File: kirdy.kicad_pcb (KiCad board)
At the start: 2 copper layers, 384 parts, among them J1 MOD_IN, J2 DNP, J3 DNP, J4 Conn_02x05_Odd_Even, J5 Barrel_Jack, J6 RJ45_Abracon_ARJP11A-MASA-B-A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, J7 USB_C_Receptacle_USB2.0, J8 Conn_02x05_Odd_Even, J9 Conn_02x05_Odd_Even, Q1 CSD17507Q5A, Q2 BSS138, Q3 BSS138, Q4 BC857, Q5 AOSP21321, Q6 BC857, SW1 SW_DIP_x03, U1 LTC6655BHLS8-4.096, U10 LT3081xDF, U11 LT3042xMSE, U12 LT3045xMSE, U13 LT3045xMSE, U14 LT3042xMSE, U15 LT3094xMSE, U16 LT3042xMSE, U17 AD5680, U18 AD7172-2, U19 RS8552, U2 MAX5719xSD, U20 MAX1968xUI, U21 ACPL-217-500E, U22 TPS54620, U23 AG5300, U24 ACPL-217-500E, U25 AMS1117-3.3, U26 LAN8742A, U27 USBLC6-4SC6, U28 USBLC6-4SC6, U3 ADA4898-1YRDZ, U4 ADA4898-1YRDZ, U5 RS8552, U6 ADA4898-1YRDZ, U7 STM32F407VGTx, U8 STM809SWX6F, U9 LTC3261, Y1 8MHz, Y2 25MHz

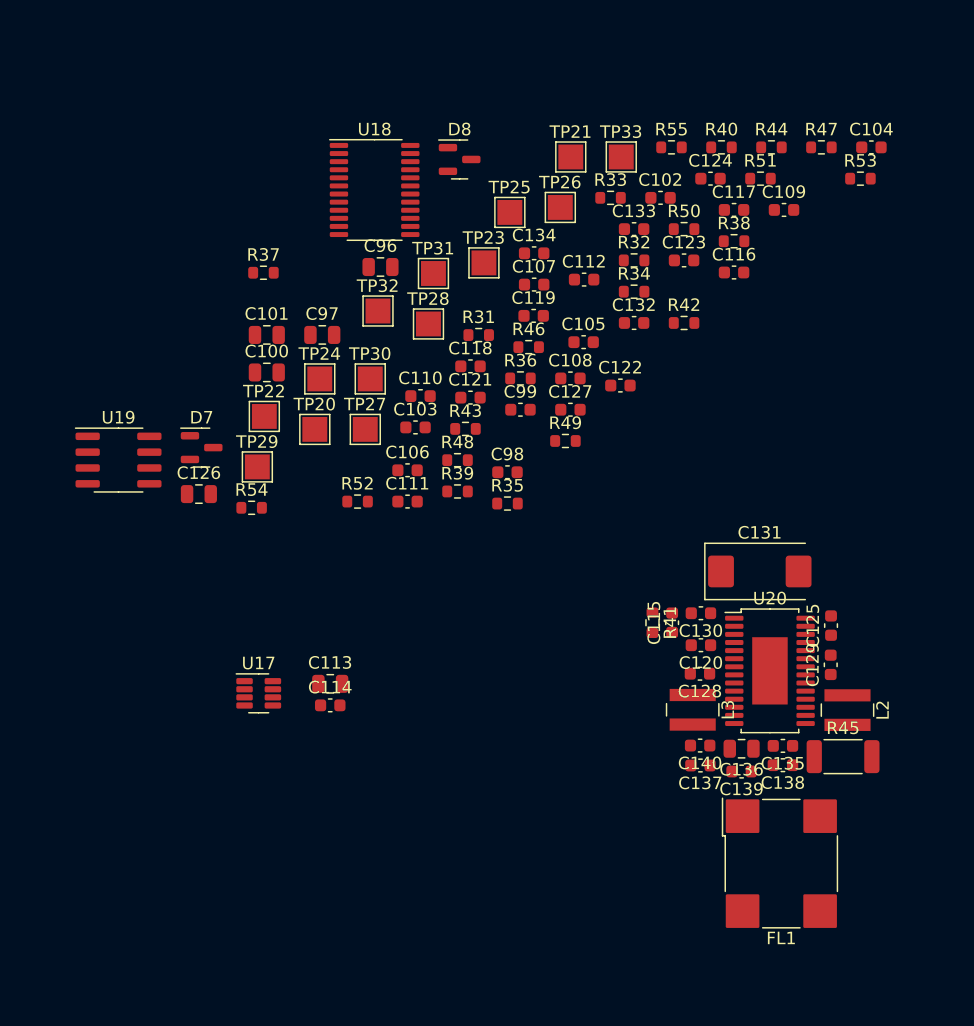
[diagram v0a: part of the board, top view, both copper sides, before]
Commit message: add bom, finish rough placement
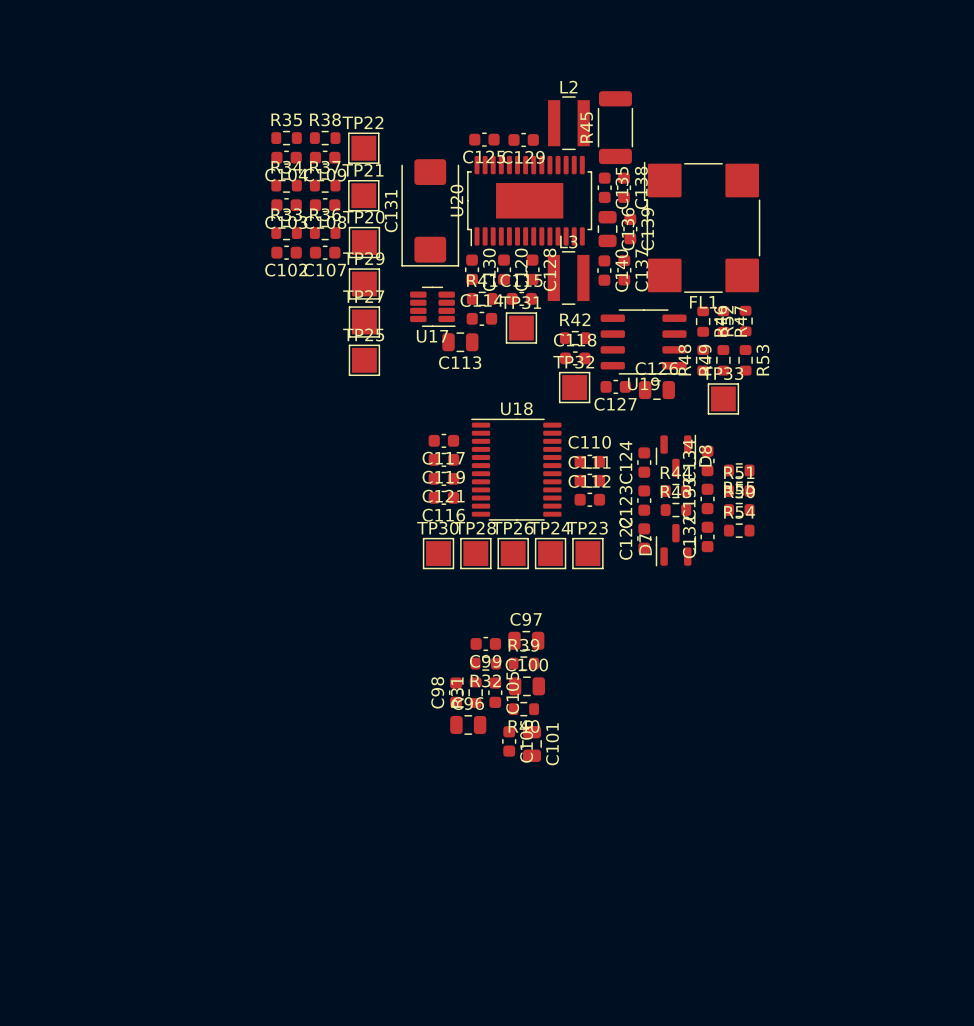
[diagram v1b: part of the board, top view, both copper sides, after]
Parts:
- FL1: value 5A -> WE-SL5
- moved R45 53.7 mm to (359.3, 86.5), turned to 90 degrees
- moved L2 52.1 mm to (355.6, 86.1), turned to 0 degrees
- moved FL1 51.4 mm to (366.4, 94.5)
- moved C129 48.8 mm to (352.0, 87.5), turned to 180 degrees
- moved C138 48.1 mm to (360.0, 91.3), turned to -90 degrees
- moved C125 47.9 mm to (348.8, 87.5), turned to 180 degrees
- moved R40 47.8 mm to (352.0, 133.1), turned to 180 degrees
- moved C135 47.0 mm to (358.5, 91.3), turned to -90 degrees
- moved C104 46.9 mm to (332.9, 88.9), turned to 180 degrees
- moved C139 44.4 mm to (360.5, 94.6), turned to -90 degrees
- moved U19 43.2 mm to (361.6, 103.7), turned to 180 degrees
- moved C136 43.1 mm to (358.7, 94.6), turned to -90 degrees
- moved U20 42.4 mm to (352.5, 92.4), turned to 90 degrees
- moved C137 40.2 mm to (360.0, 97.9), turned to -90 degrees
- moved C131 39.2 mm to (344.5, 93.2), turned to 90 degrees
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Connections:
- FL1 pad 2: /thermostat/TEC+ -> Net-(C136-Pad2)
- FL1 pad 3: Net-(C136-Pad2) -> /thermostat/TEC-
- FL1 pad 4: /thermostat/TEC- -> /thermostat/TEC+

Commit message: complete placement
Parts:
- added C173: 100n, Capacitor_SMD:C_0603_1608Metric, F.Cu at (77.8, 38.9)
- added H1: MountingHole_Pad, MountingHole:MountingHole_2.7mm_M2.5_Pad_Via, F.Cu at (3.57, 5.51)
- added H2: MountingHole_Pad, MountingHole:MountingHole_2.7mm_M2.5_Pad_Via, F.Cu at (3.56, 94.4)
- added H3: MountingHole_Pad, MountingHole:MountingHole_2.7mm_M2.5_Pad_Via, F.Cu at (156.0, 96.0)
- added H4: MountingHole_Pad, MountingHole:MountingHole_2.7mm_M2.5_Pad_Via, F.Cu at (156.0, 4.00)
- added R100: 0, Resistor_SMD:R_0603_1608Metric, F.Cu at (153.7, 91.7)
- added R101: 0, Resistor_SMD:R_0603_1608Metric, F.Cu at (156.0, 8.36)
- added R98: 0, Resistor_SMD:R_0603_1608Metric, F.Cu at (8.87, 7.83)
- added R99: 0, Resistor_SMD:R_0603_1608Metric, F.Cu at (8.56, 92.8)
- FL3: value 90R@100MHz -> Filter_EMI_LL_1423
- TP1, TP10, TP11, TP12, TP13, TP14, TP15, TP16, TP17, TP18, TP19, TP2, TP20, TP21, TP22, TP23, TP24, TP25, TP26, TP27, TP28, TP29, TP3, TP30, TP31, TP32, TP33, TP34, TP35, TP36, TP37, TP38, TP4, TP5, TP6, TP7, TP8, TP9: moved to B.Cu
- moved TP14 397.3 mm to (69.8, 31.8), turned to 180 degrees
- moved C63 395.7 mm to (72.4, 42.5), turned to 180 degrees
- moved C46 395.6 mm to (76.7, 51.5), turned to 90 degrees
- moved C83 394.9 mm to (66.3, 39.1), turned to -90 degrees
- moved C50 394.9 mm to (68.9, 46.5)
- moved C76 393.1 mm to (68.9, 34.6)
- moved C57 390.7 mm to (68.9, 44.4)
- moved TP13 390.0 mm to (78.7, 47.0), turned to 180 degrees
- moved C69 389.8 mm to (71.7, 40.1), turned to -90 degrees
- moved R23 389.7 mm to (71.7, 37.0), turned to -90 degrees
- moved C75 388.6 mm to (81.0, 41.9)
- moved C90 387.5 mm to (66.3, 35.6), turned to 90 degrees
- moved C35 387.5 mm to (88.4, 56.2), turned to -90 degrees
- moved C36 386.5 mm to (79.4, 55.5), turned to 90 degrees
- moved C66 385.2 mm to (91.8, 45.6), turned to -90 degrees
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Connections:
- net +1V8 renamed Net-(C35-Pad1)
- FL3 pad 1: Net-(FL3-Pad1) -> Net-(J7-PadA6)
- FL3 pad 2: Net-(FL3-Pad2) -> /MCU/USB_DP
- FL3 pad 3: /MCU/USB_DP -> /MCU/USB_DN
- FL3 pad 4: /MCU/USB_DN -> Net-(J7-PadA7)
- J3 pad 1: GND -> Net-(J3-Pad1)
- J7 pad A6: Net-(FL3-Pad2) -> Net-(J7-PadA6)
- J7 pad A7: Net-(FL3-Pad1) -> Net-(J7-PadA7)
- J7 pad B6: Net-(FL3-Pad2) -> Net-(J7-PadA6)
- J7 pad B7: Net-(FL3-Pad1) -> Net-(J7-PadA7)
- R13 pad 3: GND -> Net-(J3-Pad1)
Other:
- board outline added: 160 x 100 mm

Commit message: routing, bom update
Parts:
- added R102: 1k, Resistor_SMD:R_0603_1608Metric, F.Cu at (40.9, 41.1)
- moved TP23 10.3 mm to (138.4, 97.2)
- moved TP24 10.3 mm to (142.2, 97.2)
- moved TP30 10.3 mm to (134.5, 97.2)
- moved TP26 10.3 mm to (142.2, 101.0)
- moved TP28 10.3 mm to (134.5, 101.0)
- moved C169 10.2 mm to (30.5, 50.6), turned to 90 degrees
- moved TP32 7.31 mm to (121.4, 62.3)
- moved C146 5.46 mm to (39.8, 80.0), turned to 180 degrees
- moved C8 3.63 mm to (121.4, 28.3), turned to -90 degrees
- moved TP33 2.55 mm to (134.6, 64.4)
- moved R3 1.53 mm to (109.2, 26.3)
- moved C170 1.51 mm to (24.8, 59.2)
- moved D1 1.06 mm to (110.3, 10.7)
- moved R1 1.06 mm to (107.5, 11.5)
- moved R2 1.06 mm to (110.3, 12.5)
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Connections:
- J9 pad 7: /thermostat/NTC+ -> /thermostat/NTC-
- J9 pad 9: /thermostat/NTC- -> /thermostat/NTC+
- U27 pad 4: /Ehternet/PHY_TD_P -> /Ehternet/PHY_TD_N
- U27 pad 6: /Ehternet/PHY_TD_N -> /Ehternet/PHY_TD_P
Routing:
- net /MCU/TADC_SYNC: track 0.00 -> 129.7 mm, vias 0 -> 2
- net /MCU/TADC_MISO: track 0.00 -> 126.7 mm, vias 0 -> 2
- net /MCU/TADC_CLK: track 0.00 -> 125.9 mm, vias 0 -> 2
- net /MCU/TEC_VSEN: track 0.00 -> 122.4 mm, vias 0 -> 2
- net /MCU/TADC_MOSI: track 0.00 -> 122.4 mm, vias 0 -> 2
- net /MCU/TADC_CS: track 0.00 -> 120.8 mm, vias 0 -> 2
- net Net-(J1-Pad1): track 0.00 -> 118.3 mm
- net /MCU/PD_MON: track 0.00 -> 116.6 mm
- net /MCU/TEC_SHDN: track 0.00 -> 112.5 mm, vias 0 -> 2
- net /MCU/TEC_ISEN: track 0.00 -> 111.3 mm, vias 0 -> 2
- net /MCU/TDAC_MOSI: track 0.00 -> 110.5 mm, vias 0 -> 2
- net /MCU/TEC_VREF: track 0.00 -> 107.3 mm, vias 0 -> 2
- net /MCU/TDAC_CLK: track 0.00 -> 105.3 mm, vias 0 -> 2
- net /MCU/TDAC_SYNC: track 0.00 -> 101.3 mm, vias 0 -> 2
- net /MCU/PD_BIAS: track 0.00 -> 99.8 mm, vias 0 -> 2
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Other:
- copper layers 2 -> 4

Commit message: more routing
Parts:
- removed TP1, TP11, TP12, TP13, TP14, TP15, TP16, TP17, TP18, TP19, TP2, TP20, TP21, TP22, TP23, TP24, TP25, TP26, TP27, TP28, TP29, TP3, TP30, TP31, TP32, TP33, TP34, TP35, TP36, TP37, TP38, TP4, TP5, TP6, TP7, TP8: TestPoint, TestPoint:TestPoint_Pad_2.0x2.0mm
- J5: value Barrel_Jack -> Barrel_Jack_MountingPin
- R62: footprint Resistor_SMD:R_0603_1608Metric -> Resistor_SMD:R_1206_3216Metric
- moved R62 34.0 mm to (13.7, 89.5), turned to 90 degrees
- moved Q3 30.8 mm to (16.6, 89.9)
- moved R91 22.7 mm to (13.5, 52.7), turned to 90 degrees
- moved C171 20.4 mm to (16.9, 53.1)
- moved TP9 14.9 mm to (136.1, 16.8)
- moved TP10 13.1 mm to (137.9, 13.2)
- moved C152 3.57 mm to (70.9, 83.8), turned to 180 degrees
- moved C155 3.44 mm to (70.9, 79.0), turned to 180 degrees
- moved D9 2.89 mm to (14.4, 80.9)
- moved R68 2.44 mm to (76.5, 81.5)
- moved R69 2.44 mm to (76.5, 78.2)
- moved C46 2.18 mm to (74.5, 51.2)
- moved C44 2.16 mm to (78.4, 51.3)
- moved C45 2.16 mm to (76.3, 51.3)
- moved C33 2.16 mm to (73.4, 55.3)
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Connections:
- J5 pad MP: (no net) -> GND
- J6 pad 10: /Ehternet/POE_VC+ -> /Ehternet/POE_VC-
- J6 pad 9: /Ehternet/POE_VC- -> /Ehternet/POE_VC+
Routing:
- net /MCU/MCU_RSTn: track 2.15 -> 94.1 mm
- net /Ehternet/POE_VC-: track 4.02 -> 53.3 mm, vias 0 -> 2
- net /Ehternet/POE_VC+: track 0.00 -> 44.9 mm, vias 0 -> 2
- net Net-(Q3-Pad1): track 24.3 -> 56.4 mm, vias 0 -> 2
- net /Ehternet/ETH_SHIELD: track 31.8 -> 0.00 mm
- net Net-(U23-Pad3): track 0.00 -> 29.5 mm, vias 0 -> 1
- net /MCU/TEC_SHDN: track 112.5 -> 140.2 mm, vias 2 -> 4
- net /thermostat/ADC_REF: track 6.68 -> 33.7 mm, vias 0 -> 2
- net +5V: track 4.56 -> 31.3 mm, vias 0 -> 6
- net Net-(Q6-Pad1): track 0.00 -> 20.9 mm, vias 0 -> 2
- net Net-(C145-Pad2): track 19.5 -> 0.00 mm
- net /MCU/TDAC_MOSI: track 110.5 -> 126.4 mm
- net /MCU/TDAC_CLK: track 105.3 -> 121.3 mm
- net /MCU/TDAC_SYNC: track 101.3 -> 117.3 mm
- net Net-(C146-Pad1): track 0.00 -> 15.7 mm, vias 0 -> 2
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- added copper zone on F.Cu, net +12V
- added copper zone on F.Cu, net +15V
- added copper zone on F.Cu, net +3.3VA
- added copper zone on F.Cu, net +5V
- added copper zone on F.Cu, net +5VA
- added copper zone on F.Cu, net +8V
- added copper zone on F.Cu, net +9V
- added copper zone on F.Cu, net +9VA
- added copper zone on F.Cu, net -6V
- added copper zone on F.Cu, net -9V
- added copper zone on B.Cu, net /Ehternet/ETH_SHIELD
- added copper zone on F.Cu, net /Ehternet/ETH_SHIELD
- added copper zone on F.Cu, net /Ehternet/POE_VC+
- added copper zone on F.Cu, net /Ehternet/POE_VC-
- added copper zone on F.Cu, net /driveStage/LD-
- added copper zone on F.Cu, net /thermostat/TEC+
- added copper zone on F.Cu, net /thermostat/TEC-
- added copper zone on In1.Cu, net GND
- added copper zone on F.Cu, net IN
- added copper zone on F.Cu, net Net-(C135-Pad2)
- added copper zone on F.Cu, net Net-(C136-Pad2)
- added copper zone on F.Cu, net Net-(C141-Pad1)
- added copper zone on F.Cu, net Net-(C145-Pad1)
- added copper zone on F.Cu, net Net-(C145-Pad2)
- added copper zone on F.Cu, net Net-(C146-Pad1)
- added copper zone on F.Cu, net Net-(C148-Pad1)
- added copper zone on F.Cu, net Net-(C149-Pad2)
- added copper zone on F.Cu, net Net-(C152-Pad1)
- added copper zone on F.Cu, net Net-(C152-Pad2)
- added copper zone on F.Cu, net Net-(C35-Pad1)
- added copper zone on F.Cu, net Net-(C37-Pad2)
- added copper zone on F.Cu, net Net-(C40-Pad1)
- added copper zone on F.Cu, net Net-(C42-Pad2)
- added copper zone on F.Cu, net Net-(C43-Pad2)
- added copper zone on F.Cu, net Net-(C50-Pad1)
- added copper zone on F.Cu, net Net-(C51-Pad1)
- added copper zone on F.Cu, net Net-(C52-Pad1)
- added copper zone on F.Cu, net Net-(C53-Pad1)
- added copper zone on F.Cu, net Net-(C54-Pad1)
- added copper zone on F.Cu, net Net-(C55-Pad1)
- added copper zone on F.Cu, net Net-(L2-Pad1)
- added copper zone on F.Cu, net Net-(L3-Pad1)
- added copper zone on F.Cu, net Net-(Q1-Pad1)
- added copper zone on F.Cu, net Net-(R45-Pad1)

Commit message: roughly done
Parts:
- TP10, TP9: moved to F.Cu
- moved TP9 7.73 mm to (130.4, 11.6), turned to 0 degrees
- moved R98 5.62 mm to (3.56, 9.65)
- moved R99 5.60 mm to (3.56, 90.3)
- moved TP10 4.62 mm to (133.6, 11.6), turned to 0 degrees
- moved R100 2.39 mm to (156.1, 91.6), turned to 180 degrees
- moved L2 0.22 mm to (120.6, 68.1)
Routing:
- net GND: track 16.4 -> 377.1 mm, vias 0 -> 441
- net +3V3: track 21.9 -> 48.2 mm, vias 0 -> 41
- net Net-(U19-Pad5): track 0.00 -> 18.8 mm, vias 0 -> 2
- net +3.3VA: track 3.90 -> 17.3 mm, vias 0 -> 15
- net Net-(R10-Pad2): track 1.78 -> 10.5 mm
- net Net-(Q5-Pad4): track 2.15 -> 8.06 mm
- net Net-(J2-Pad1): track 7.66 -> 13.2 mm
- net +5VA: track 13.7 -> 19.3 mm, vias 0 -> 9
- net Net-(H3-Pad1): track 0.00 -> 4.81 mm
- net Net-(H4-Pad1): track 0.00 -> 4.71 mm
- net Net-(H1-Pad1): track 0.00 -> 4.49 mm
- net Net-(H2-Pad1): track 0.00 -> 4.46 mm
- net /MCU/PD_BIAS: track 99.9 -> 103.4 mm
- net -6V: track 15.9 -> 13.5 mm, vias 0 -> 29
- net +9VA: track 10.3 -> 12.5 mm, vias 0 -> 9
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- added copper zone on In2.Cu, net +12V
- added copper zone on B.Cu, net +15V
- added copper zone on In2.Cu, net +3.3VA
- added copper zone on F.Cu, net +3V3
- added copper zone on In2.Cu, net +3V3
- added copper zone on In2.Cu, net +5V
- added copper zone on In2.Cu, net +5VA
- added copper zone on In2.Cu, net +9V
- added copper zone on B.Cu, net +9VA
- added copper zone on In2.Cu, net -6V
- added copper zone on F.Cu, net Net-(C158-Pad1)

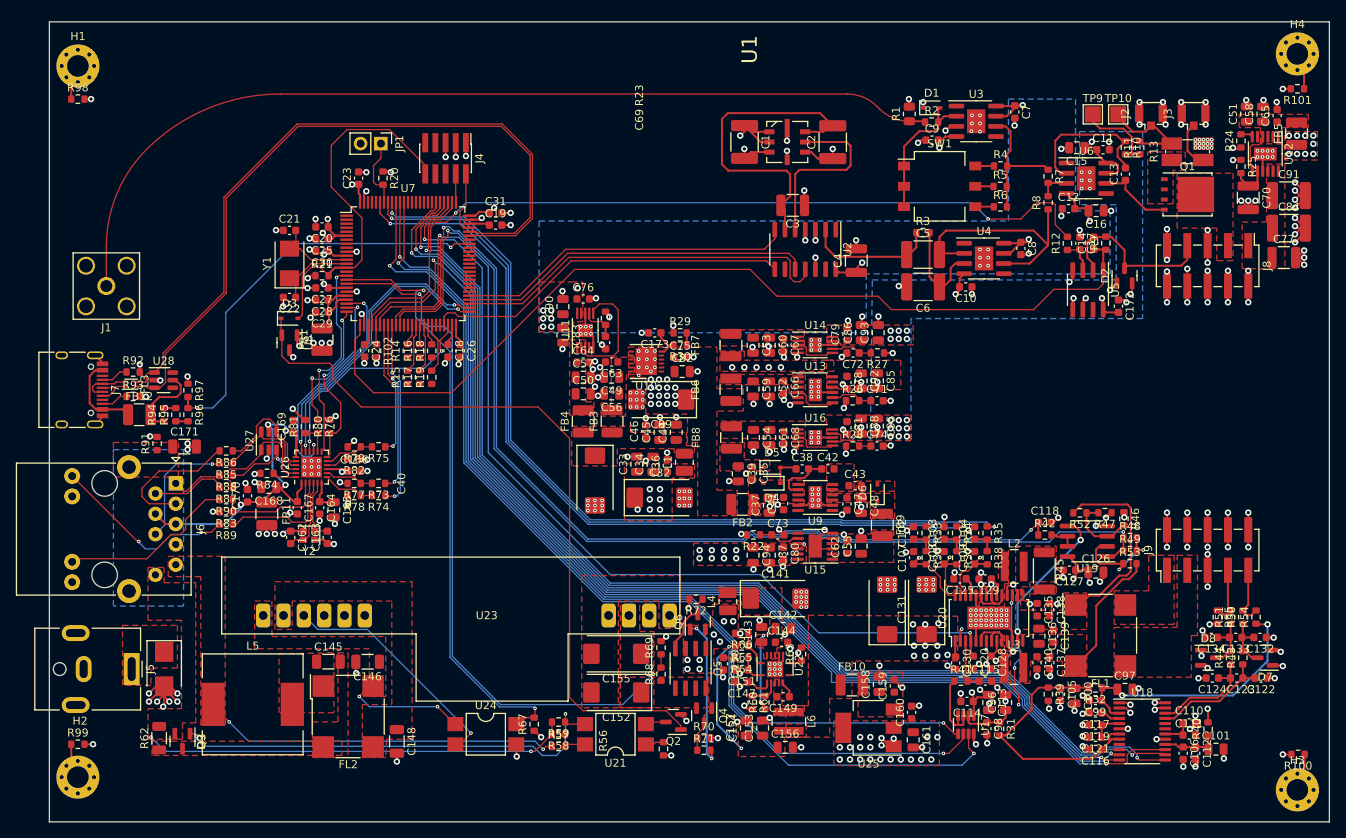
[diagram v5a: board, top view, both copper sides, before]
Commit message: passes DRC
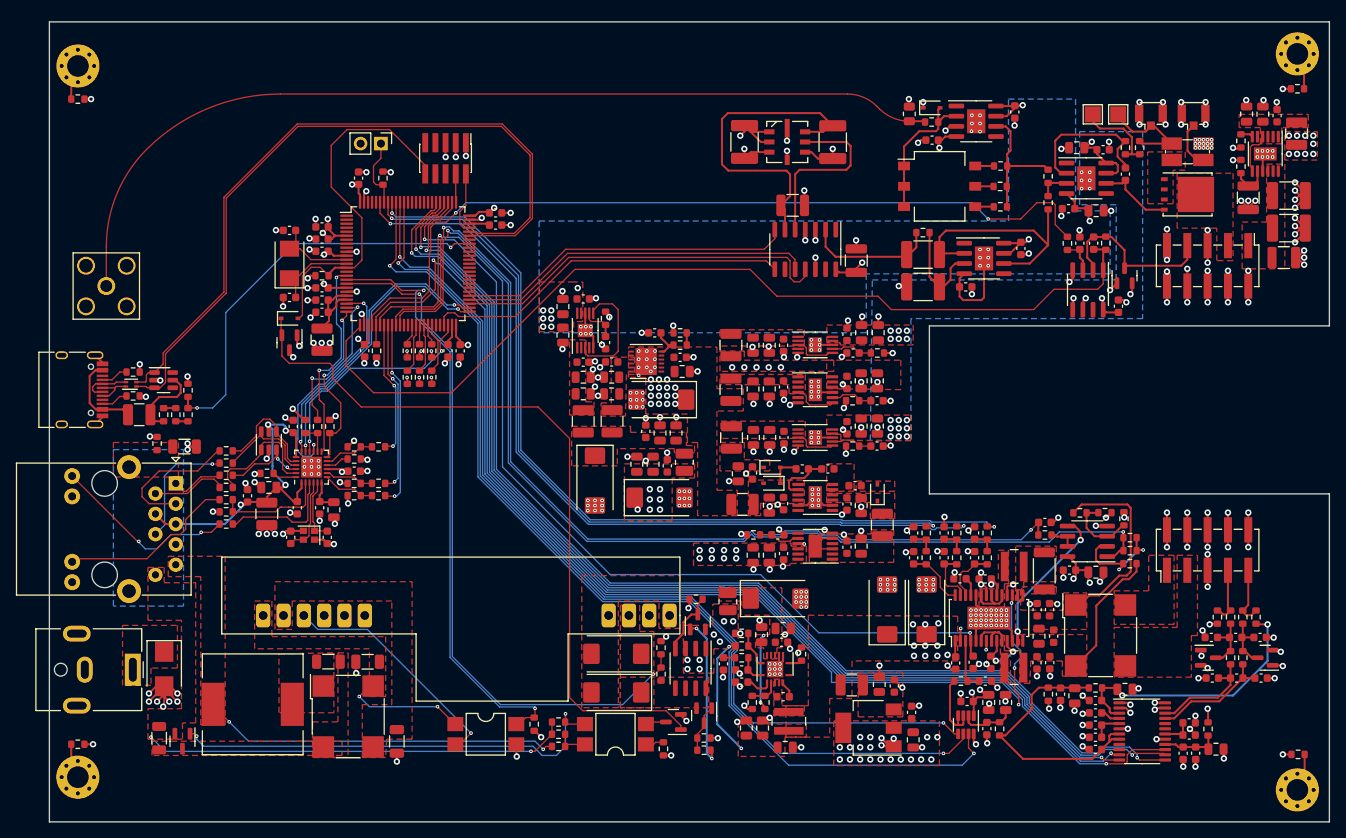
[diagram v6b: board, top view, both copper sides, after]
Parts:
- moved J5 0.16 mm to (10.4, 81.0)
- moved C44 0.08 mm to (78.3, 51.4)
- moved C45 0.08 mm to (76.3, 51.4)
- moved R93 0.06 mm to (10.5, 46.8)
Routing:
- net -6V: track 13.5 -> 21.8 mm, vias 29 -> 28
- net +3V3: track 48.2 -> 54.9 mm, vias 41 -> 49
- net /MCU/POE_PWR_SRC: track 90.0 -> 88.8 mm
- net /thermostat/MAXIP: track 8.24 -> 7.12 mm, vias 1 -> 0
- net /thermostat/MAXIN: track 8.01 -> 6.91 mm, vias 1 -> 0
- net /thermostat/MAXV: track 8.65 -> 7.55 mm, vias 1 -> 0
- net /MCU/PD_MON: track 116.6 -> 117.5 mm
- net GND: track 377.1 -> 377.9 mm, vias 441 -> 442
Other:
- outline, holes or cut-outs redrawn
